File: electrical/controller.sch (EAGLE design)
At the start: 35 parts, among them IC1 555, IC2 MCP4728, Q1 IRLIB9343PBF-ND, Q3 600mA/40V, U1 POLOLU_D24V22F5, U5 MCP6142

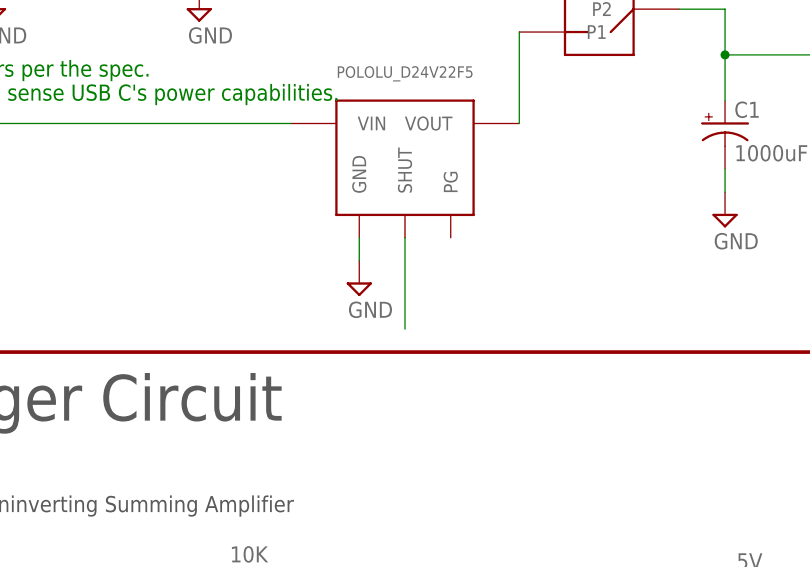
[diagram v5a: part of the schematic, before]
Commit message: Create 3d model of PCB from Eagle
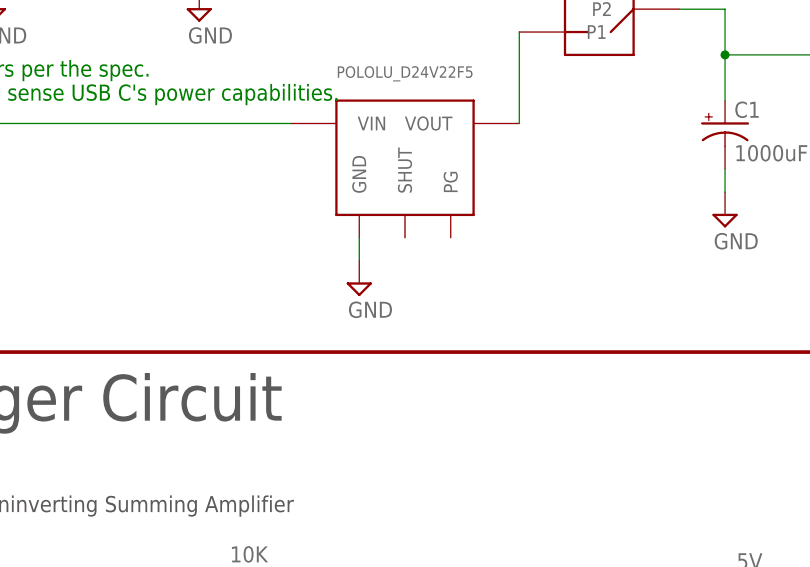
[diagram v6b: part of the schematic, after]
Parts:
- J1: device SparkFun-Connectors:USB_C_2-LAYER_PADS -> BEST_Custom:USB_C_2-LAYER_PADS
- Q1: device transistor-fet:IRF9530 -> BEST_Custom:IRF9530
- S1, S2, S3, S4: device pie:TAC_SWITCHPTH -> BEST_Custom:TAC_SWITCHPTH
- ST1, ST2: device pie:2PIN_SCREW -> BEST_Custom:2PIN_SCREW
- S_PWR: device custom_parts:SPDT_TOGGLE_SWITCH -> BEST_Custom:SPDT_TOGGLE_SWITCH
- U1: device custom_parts:POLOLU_D24V22F5 -> BEST_Custom:POLOLU_D24V22F5
- UC1: device pie:ARDUINO_PRO_MICRO -> BEST_Custom:ARDUINO_PRO_MICRO
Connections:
- removed net N$1: U1.SHUT
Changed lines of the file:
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@@
 <attribute name="REVISION" value="D1"/>
 </part>
-<part name="UC1" library="pie" deviceset="ARDUINO_PRO_MICRO" device=""/>
-<part name="ST1" library="pie" deviceset="2PIN_SCREW" device=""/>
-<part name="ST2" library="pie" deviceset="2PIN_SCREW" device=""/>
+<part name="UC1" library="BEST_Custom" library_urn="urn:adsk.eagle:library:10805467" deviceset="ARDUINO_PRO_MICRO" device=""/>
+<part name="ST1" library="BEST_Custom" library_urn="urn:adsk.eagle:library:10805467" deviceset="2PIN_SCREW" device="" package3d_urn="urn:adsk.eagle:package:49052268/2"/>
+<part name="ST2" library="BEST_Custom" library_urn="urn:adsk.eagle:library:10805467" deviceset="2PIN_SCREW" device="" package3d_urn="urn:adsk.eagle:package:49052268/2"/>
 <part name="U5" library="linear" library_urn="urn:adsk.eagle:library:262" deviceset="MCP602" device="P" package3d_urn="urn:adsk.eagle:package:16409/2" value="MCP6142"/>
 <part name="SUPPLY1" library="pie" deviceset="GND" device=""/>
@@
 <part name="U$10" library="pie" deviceset="5V" device=""/>
 <part name="R7" library="pie" deviceset="R-US_" device="R0603" value="10K"/>
-<part name="S4" library="pie" deviceset="TAC_SWITCH" device="PTH"/>
-<part name="S1" library="pie" deviceset="TAC_SWITCH" device="PTH"/>
-<part name="S2" library="pie" deviceset="TAC_SWITCH" device="PTH"/>
+<part name="S4" library="BEST_Custom" library_urn="urn:adsk.eagle:library:10805467" deviceset="TAC_SWITCH" device="PTH" package3d_urn="urn:adsk.eagle:package:49052242/2"/>
+<part name="S1" library="BEST_Custom" library_urn="urn:adsk.eagle:library:10805467" deviceset="TAC_SWITCH" device="PTH" package3d_urn="urn:adsk.eagle:package:49052242/2"/>
+<part name="S2" library="BEST_Custom" library_urn="urn:adsk.eagle:library:10805467" deviceset="TAC_SWITCH" device="PTH" package3d_urn="urn:adsk.eagle:package:49052242/2"/>
 <part name="SUPPLY13" library="pie" deviceset="GND" device=""/>
 <part name="SUPPLY14" library="pie" deviceset="GND" device=""/>
 <part name="SUPPLY15" library="pie" deviceset="GND" device=""/>
 <part name="SUPPLY16" library="pie" deviceset="GND" device=""/>
-<part name="S_PWR" library="custom_parts" deviceset="SPDT_TOGGLE_SWITCH" device=""/>
+<part name="S_PWR" library="BEST_Custom" library_urn="urn:adsk.eagle:library:10805467" deviceset="SPDT_TOGGLE_SWITCH" device="" package3d_urn="urn:adsk.eagle:package:49052299/2"/>
 <part name="U$1" library="pie" deviceset="5V" device=""/>
 <part name="SUPPLY18" library="pie" deviceset="GND" device=""/>
-<part name="Q1" library="transistor-fet" library_urn="urn:adsk.eagle:library:396" deviceset="IRF9530" device="" package3d_urn="urn:adsk.eagle:package:28520/1" value="IRLIB9343PBF-ND "/>
+<part name="Q1" library="BEST_Custom" library_urn="urn:adsk.eagle:library:10805467" deviceset="IRF9530" device="" package3d_urn="urn:adsk.eagle:package:49053510/2" value="IRLIB9343PBF-ND "/>
 <part name="U$13" library="pie" deviceset="5V" device=""/>
 <part name="SUPPLY19" library="pie" deviceset="GND" device=""/>
-<part name="S3" library="pie" deviceset="TAC_SWITCH" device="PTH"/>
+<part name="S3" library="BEST_Custom" library_urn="urn:adsk.eagle:library:10805467" deviceset="TAC_SWITCH" device="PTH" package3d_urn="urn:adsk.eagle:package:49052242/2"/>
 <part name="SUPPLY17" library="pie" deviceset="GND" device=""/>
-<part name="U1" library="custom_parts" deviceset="POLOLU_D24V22F5" device=""/>
+<part name="U1" library="BEST_Custom" library_urn="urn:adsk.eagle:library:10805467" deviceset="POLOLU_D24V22F5" device="" package3d_urn="urn:adsk.eagle:package:49053444/2"/>
 <part name="SUPPLY20" library="pie" deviceset="GND" device=""/>
-<part name="C1" library="SparkFun-Capacitors" deviceset="CAP_POL" device="PTH4" value="1000uF"/>
-<part name="STANDOFF1" library="BEST_Custom" library_urn="urn:adsk.eagle:library:10805467" deviceset="STAND-OFF" device="KEYSTONE_SMT_STANDOFF"/>
-<part name="STANDOFF2" library="BEST_Custom" library_urn="urn:adsk.eagle:library:10805467" deviceset="STAND-OFF" device="KEYSTONE_SMT_STANDOFF"/>
-<part name="J1" library="SparkFun-Connectors" deviceset="USB_C" device="_2-LAYER_PADS"/>
+<part name="C1" library="SparkFun-Capacitors" deviceset="CAP_POL" device="PTH4" override_package3d_urn="urn:adsk.eagle:package:49053456/2" override_package_urn="urn:adsk.eagle:footprint:49053457/1" value="1000uF"/>
+<part name="STANDOFF1" library="BEST_Custom" library_urn="urn:adsk.eagle:library:10805467" deviceset="STAND-OFF" device="KEYSTONE_SMT_STANDOFF" package3d_urn="urn:adsk.eagle:package:49038533/2"/>
+<part name="STANDOFF2" library="BEST_Custom" library_urn="urn:adsk.eagle:library:10805467" deviceset="STAND-OFF" device="KEYSTONE_SMT_STANDOFF" package3d_urn="urn:adsk.eagle:package:49038533/2"/>
+<part name="J1" library="BEST_Custom" library_urn="urn:adsk.eagle:library:10805467" deviceset="USB_C" device="_2-LAYER_PADS" package3d_urn="urn:adsk.eagle:package:49053406/2"/>
 <part name="R8" library="pie" deviceset="R-US_" device="R0603" value="5.1K"/>
 <part name="R9" library="pie" deviceset="R-US_" device="R0603" value="5.1K"/>
 <part name="SUPPLY2" library="pie" deviceset="GND" device=""/>
-<part name="IC1" library="SparkFun-IC-Special-Function" deviceset="555" device="D" value="555"/>
+<part name="IC1" library="SparkFun-IC-Special-Function" deviceset="555" device="D" override_package3d_urn="urn:adsk.eagle:package:49052288/2" override_package_urn="urn:adsk.eagle:footprint:49052289/1" value="555"/>
 <part name="U$8" library="pie" deviceset="5V" device=""/>
 <part name="C6" library="BEST_Custom" library_urn="urn:adsk.eagle:library:10805467" deviceset="CAP" device="0603-CAP" package3d_urn="urn:adsk.eagle:package:10805924/1" value="0.01 uF"/>
@@
 <part name="R11" library="pie" deviceset="R-US_" device="R0603" value="2.2M"/>
 <part name="SUPPLY23" library="pie" deviceset="GND" device=""/>
-<part name="Q3" library="SparkFun-DiscreteSemi" deviceset="TRANS_PNP" device="-MMBT4403" value="600mA/40V"/>
-<part name="IC2" library="BEST_Custom" library_urn="urn:adsk.eagle:library:10805467" deviceset="MCP4728" device=""/>
+<part name="Q3" library="SparkFun-DiscreteSemi" deviceset="TRANS_PNP" device="-MMBT4403" override_package3d_urn="urn:adsk.eagle:package:49053453/2" override_package_urn="urn:adsk.eagle:footprint:49053454/1" value="600mA/40V"/>
+<part name="IC2" library="BEST_Custom" library_urn="urn:adsk.eagle:library:10805467" deviceset="MCP4728" device="" package3d_urn="urn:adsk.eagle:package:49052248/1"/>
 <part name="U$11" library="pie" deviceset="5V" device=""/>
 <part name="SUPPLY24" library="pie" deviceset="GND" device=""/>
@@
 </segment>
 </net>
-<net name="N$1" class="0">
-<segment>
-<pinref part="U1" gate="G$1" pin="SHUT"/>
-<wire x1="76.2" y1="124.46" x2="76.2" y2="134.62" width="0.1524" layer="91"/>
-</segment>
-</net>
 <net name="N$3" class="0">
 <segment>
@@
 packages will not be understood (or retained) with this version.
 </note>
+<note version="9.4" severity="warning">
+Since Version 9.4, EAGLE supports the overriding of 3D packages
+in schematics and board files. Those overridden 3d packages
+will not be understood (or retained) with this version.
+</note>
 </compatibility>

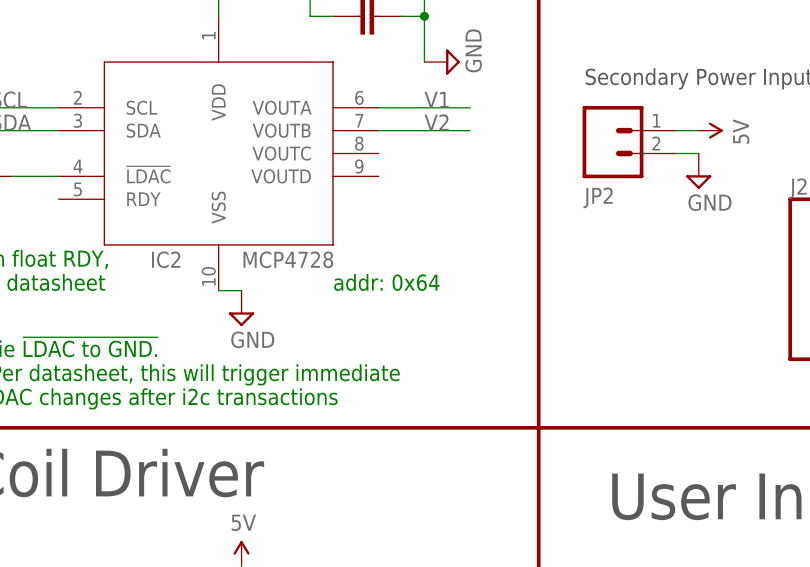
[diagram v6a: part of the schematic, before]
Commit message: Correct comment on SCH
Yes, the i2c address is reconfigurable, but hte default is 0x60
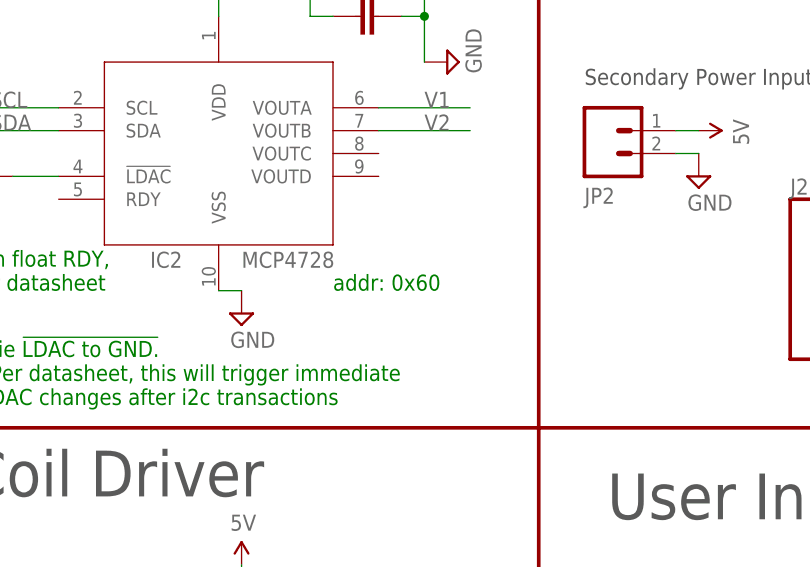
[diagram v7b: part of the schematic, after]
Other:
- note added: "addr: 0x60"
- note removed: "addr: 0x64"
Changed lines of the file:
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@@
 - We therefore use a software bit-banging approach for i2c.
 Used to be 6 SDA, 7 SCL, now we'll use 6 &amp; 8 to leave all interrupts free.</text>
-<text x="172.72" y="129.54" size="1.778" layer="91">addr: 0x64</text>
+<text x="172.72" y="129.54" size="1.778" layer="91">addr: 0x60</text>
 <text x="17.78" y="149.86" size="1.778" layer="91">5.1K resistors per the spec.
 Allows uC to sense USB C's power capabilities.</text>

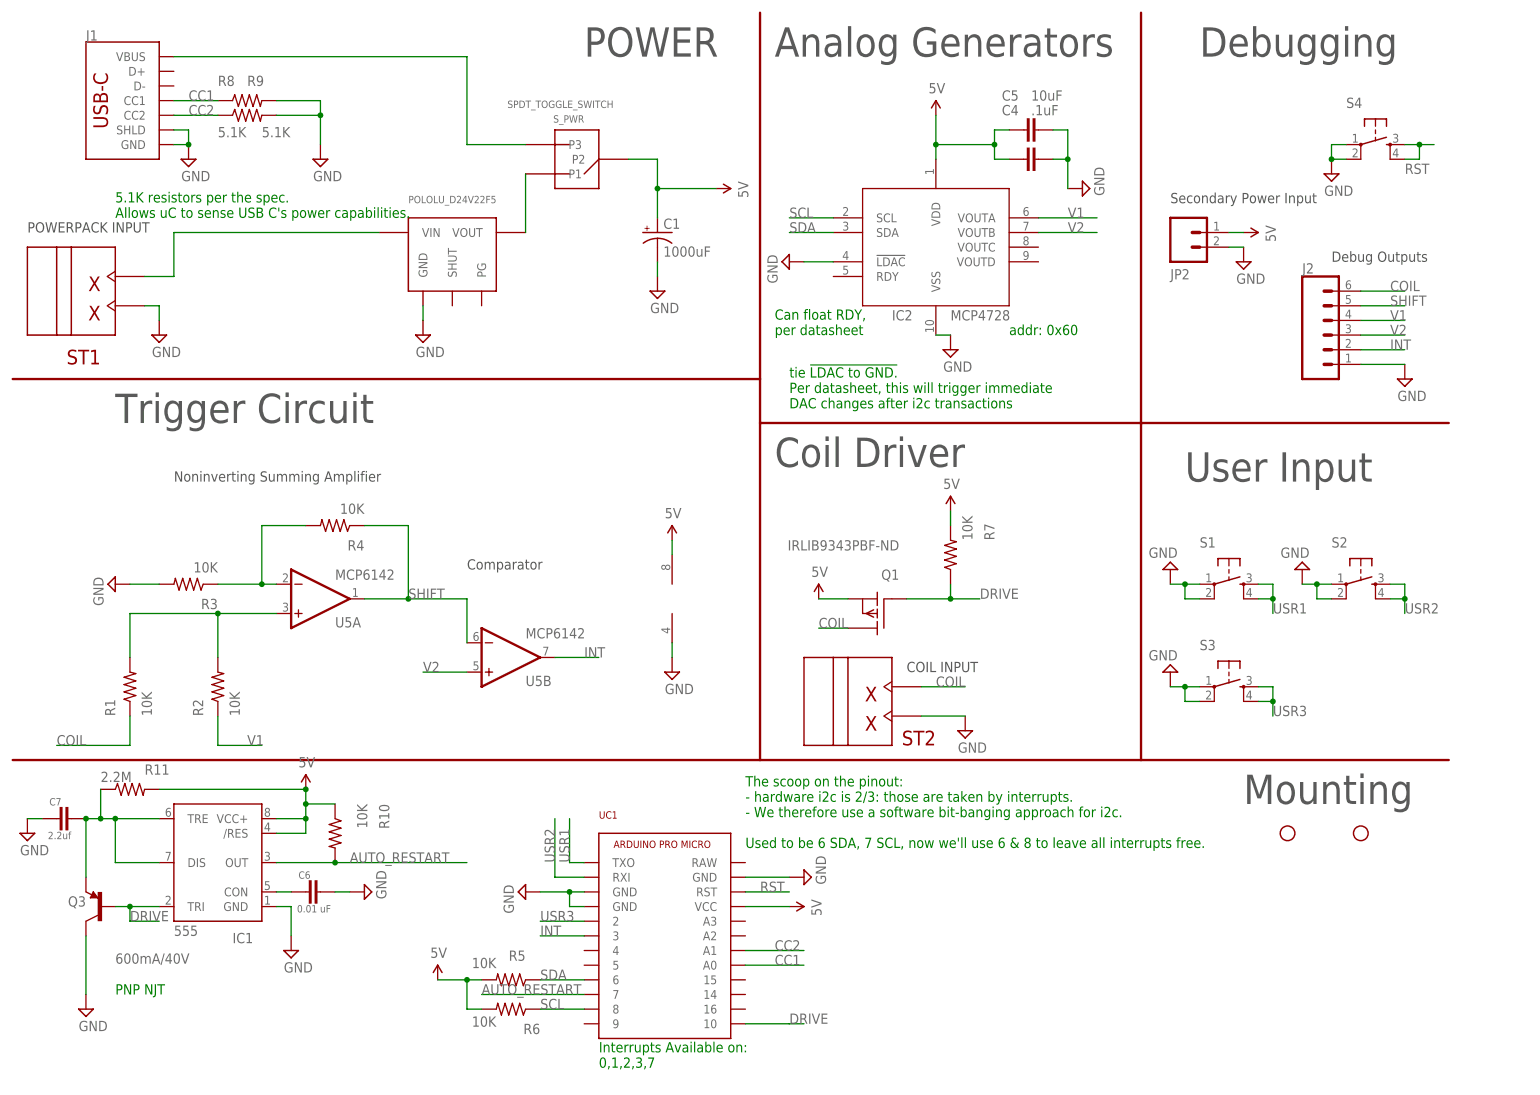
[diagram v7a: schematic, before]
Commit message: some but not all of the changes for Rev D2
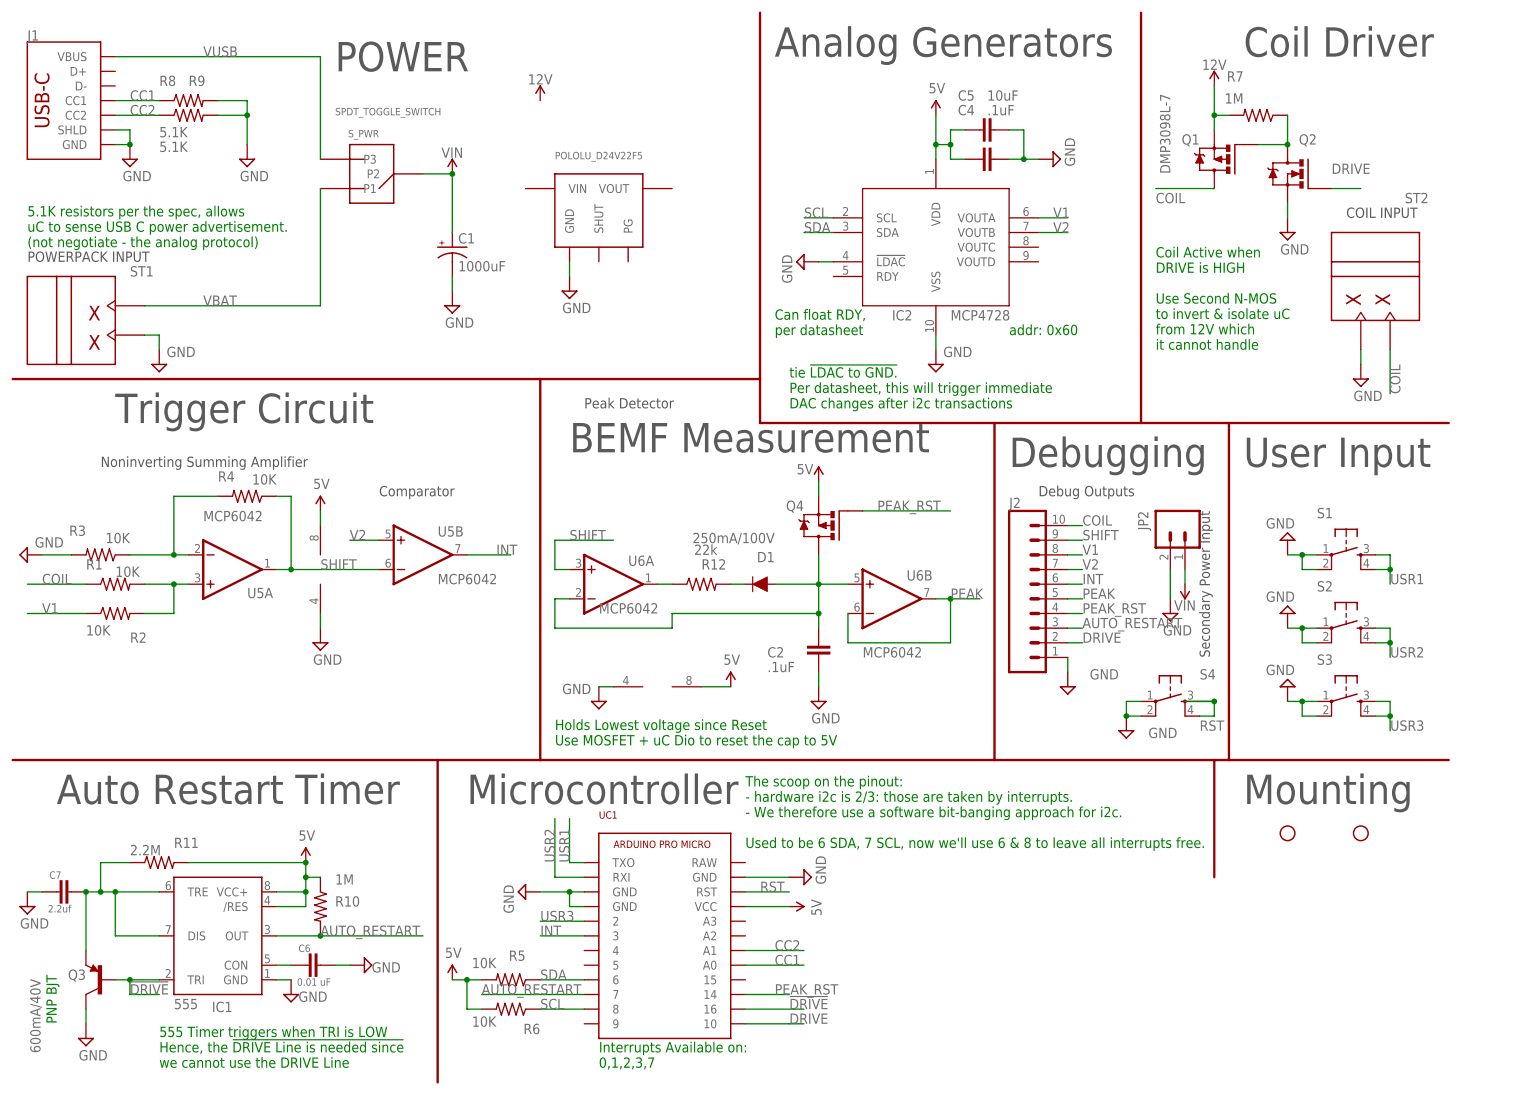
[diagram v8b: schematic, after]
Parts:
- added C2: .1uF, pie:CAP0603-CAP
- added D1: 250mA/100V, SparkFun-DiscreteSemi:DIODE-BAS16J
- added Q2: N-CHANNEL-MOSFETSOT23-3, BEST_Custom:N-CHANNEL-MOSFETSOT23-3
- added Q4: DMP3098, BEST_Custom:P-CHANNEL-MOSFETSOT23-3
- added R12: 22k, pie:R-US_R0603
- added U6: MCP6042, linear:MCP602SN
- J2: device SparkFun-Connectors:CONN_06NO_SILK_FEMALE_PTH -> SparkFun-Connectors:CONN_10"
- Q1: value IRLIB9343PBF-ND -> DMP3098; device BEST_Custom:IRF9530 -> BEST_Custom:P-CHANNEL-MOSFETSOT23-3
- R10, R7: value 10K -> 1M
- U5: value MCP6142 -> MCP6042; device linear:MCP602P -> linear:MCP602SN
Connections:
- net N$2 renamed VUSB
- new net !DRIVE: IC1.TRI, Q3.B, UC1.16
- new net 12V: Q1.S, R7.2
- new net N$1: C2.1, D1.A, Q4.D, U6A.-IN, U6B.+IN
- new net N$2: R12.1, U6A.OUT
- new net PEAK: J2.5, U6B.-IN, U6B.OUT
- new net PEAK_RST: J2.4, Q4.G, UC1.14
- new net VIN: C1.+, JP2.1, S_PWR.P2
- net 5V: now also Q4.S, U6P.V+; no longer C1.+, JP2.1, Q1.S, R7.2, S_PWR.P2
- net AUTO_RESTART: now also J2.3
- net COIL: now also J2.10; no longer J2.6
- net DRIVE: now also J2.2, Q2.D, Q2.G; no longer IC1.TRI, Q3.B
- net GND: now also C2.2, Q2.S@2, U6P.V-
- net INT: now also J2.6; no longer J2.2
- net N$3: now also D1.C, R12.2; no longer S_PWR.P1, U1.VOUT
- net SHIFT: now also J2.9, U6A.+IN; no longer J2.5
- net V1: now also J2.8; no longer J2.4
- net V2: now also J2.7; no longer J2.3
- net VBAT: now also S_PWR.P1; no longer U1.VIN
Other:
- note added: "5.1K resistors per the spec, allows uC to sense USB C power advertisement. (not negotiate - the analog protocol)"
- note added: "555 Timer triggers when TRI is LOW Hence, the !DRIVE Line is needed since we cannot use the DRIVE Line"
- note added: "Auto Restart Timer"
- note added: "BEMF Measurement"
- note added: "Coil Active when DRIVE is HIGH Use Second N-MOS to invert & isolate uC from 12V which it cannot handle"
- note added: "DMP3098L-7"
- note added: "Holds Lowest voltage since Reset Use MOSFET + uC Dio to reset the cap to 5V"
- note added: "Microcontroller"
- note added: "PNP BJT"
- note added: "Peak Detector"
- note added: "TODO: CAD & add the 12V / 5V regulators Pololu D45V1E1F5 and U3V16F12"
- note added: "TODO: Gain math for Coil to reduce the BEMF by 3x"
- note removed: "5.1K resistors per the spec. Allows uC to sense USB C's power capabilities."
- note removed: "PNP NJT"
- moved on the sheet: C1, C4, C5, C6, C7, IC1, J1, JP2, Q3, R1, R10, R11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
